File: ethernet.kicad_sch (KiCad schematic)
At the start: 43 parts, among them J4 ARJM11D7-502-AB-EW2, U1 MIMX8MM6DVTLZAA, U13 TPD4EUSB30, U14 TPD4EUSB30, U18 RTL8211FD

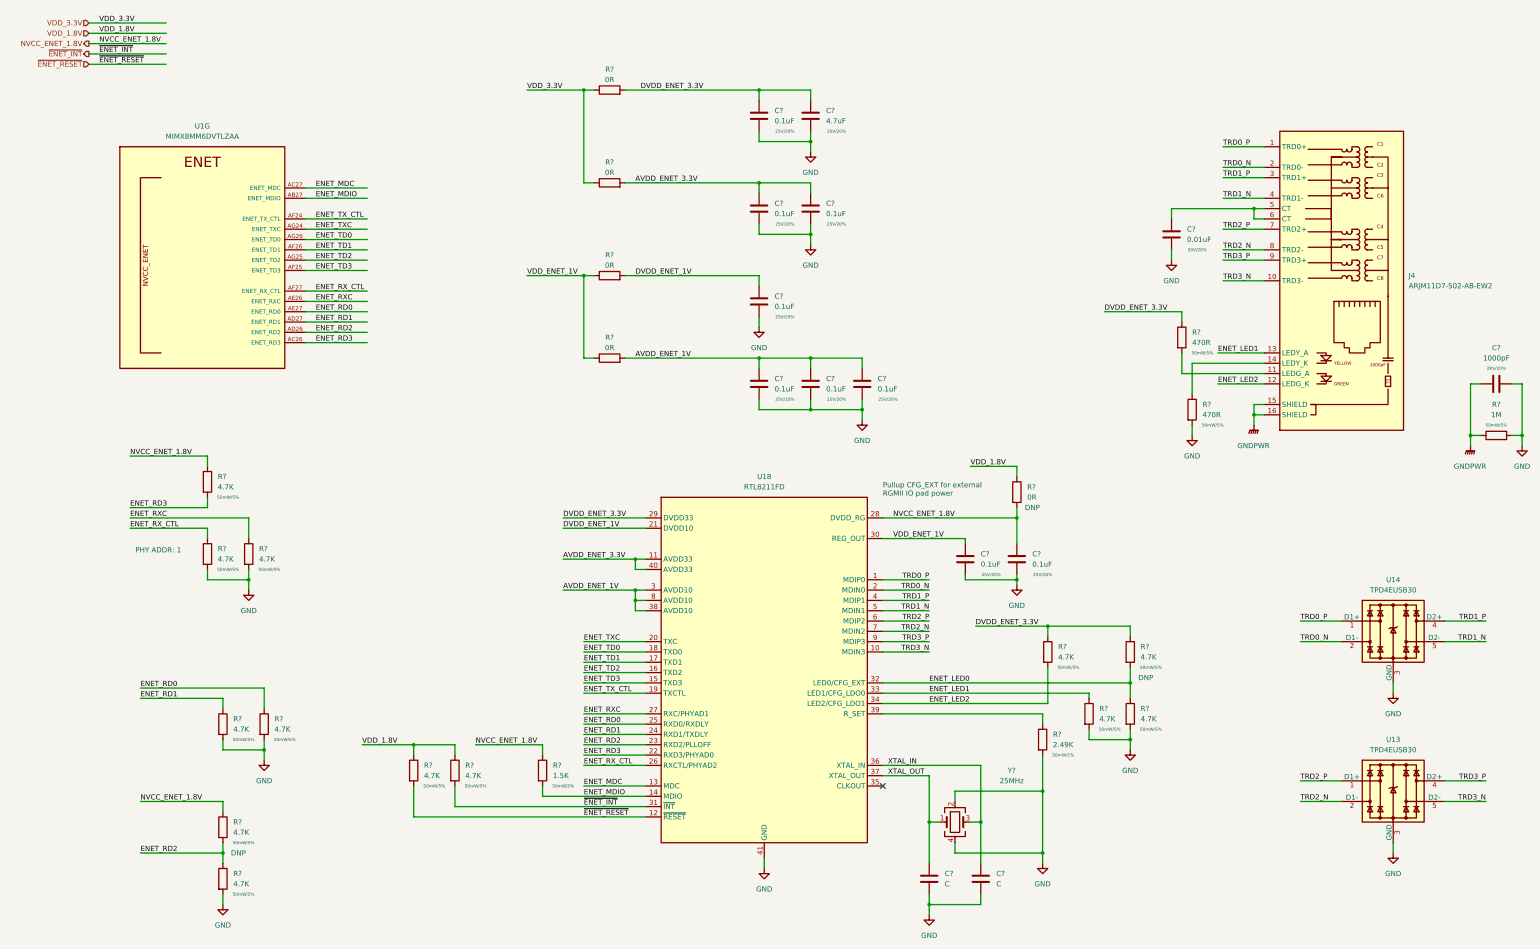
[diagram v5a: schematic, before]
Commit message: pcie done, misc fixes for usb, enet
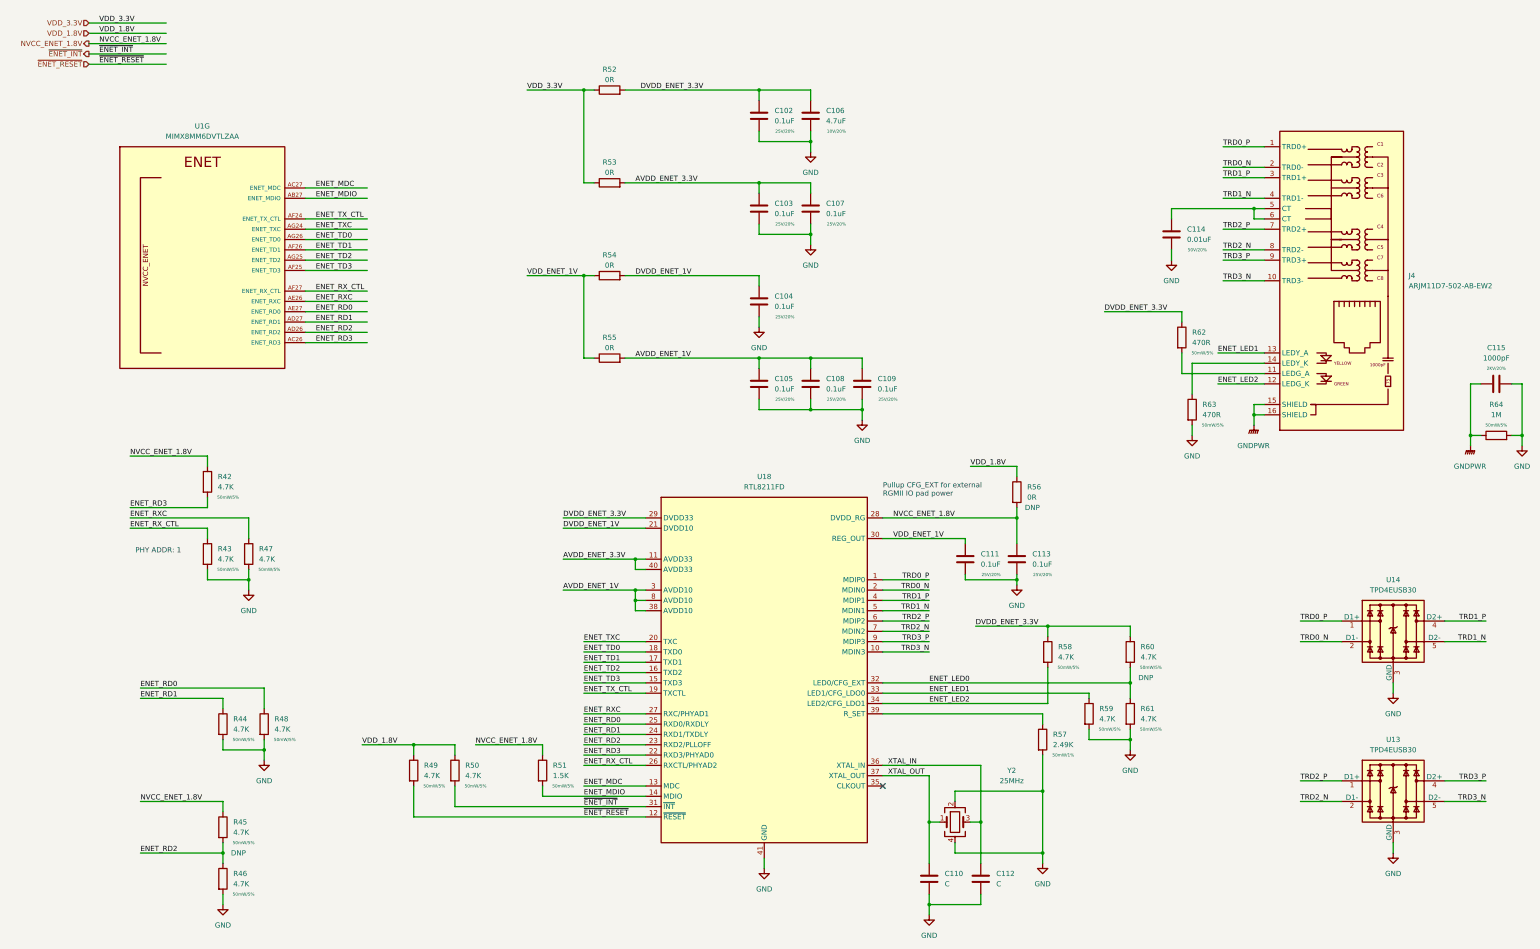
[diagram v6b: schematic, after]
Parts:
- gave numbers to parts that had none: 38

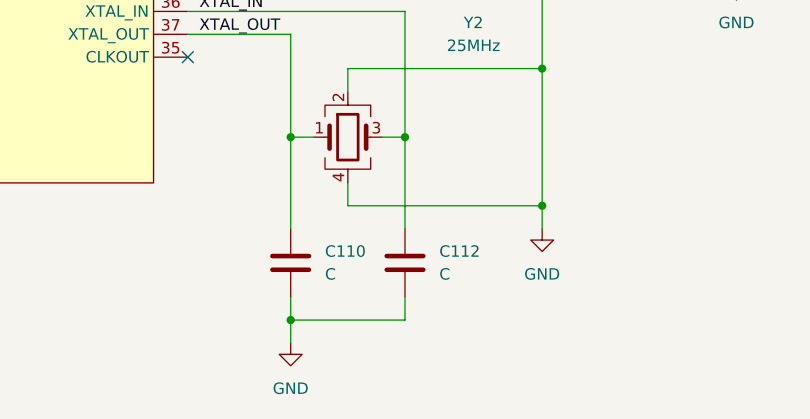
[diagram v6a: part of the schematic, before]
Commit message: ddr: add dual die support, misc work
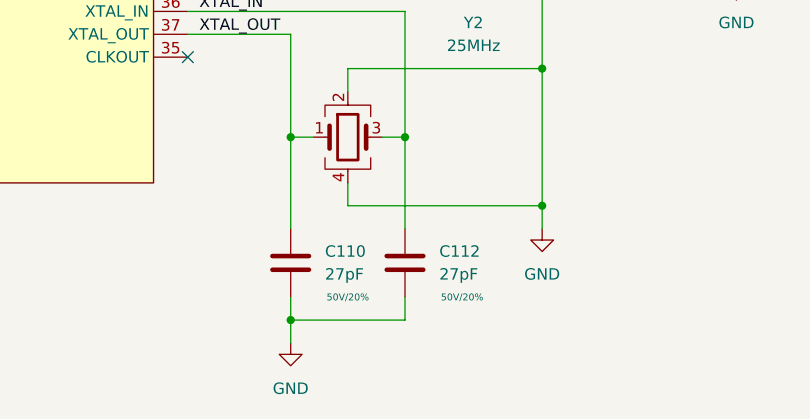
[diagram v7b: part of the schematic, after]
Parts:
- C110, C112: value C -> 27pF; Rating (none) -> 50V/20%
- Y2: footprint (none) -> Crystal:Crystal_SMD_3225-4Pin_3.2x2.5mm
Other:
- company: (none) -> Q-LAB
- title: (none) -> QSBC
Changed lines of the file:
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@@
 (kicad_sch (version 20211123) (generator eeschema)
   (paper "A3")
+  (title_block
+    (title "QSBC")
+    (rev "1")
+    (company "Q-LAB")
+  )
   (junction (at 210.82 115.57) (diameter 0) (color 0 0 0 0)
   )
@@
     )
     (pin "1")
+  )
+  (symbol (lib_id "Device:C") (at 240.03 231.14 0) (unit 1)
+    (in_bom yes) (on_board yes)
+    (property "Reference" "C110" (id 0) (at 243.84 229.8699 0)
+      (effects (font (size 1.27 1.27)) (justify left))
+    )
+    (property "Value" "27pF" (id 1) (at 243.84 232.4099 0)
+      (effects (font (size 1.27 1.27)) (justify left))
+    )
+    (property "Footprint" "Capacitor_SMD:C_0402_1005Metric" (id 2) (at 240.9952 234.95 0)
+      (effects (font (size 1.27 1.27)) hide)
+    )
+    (property "Datasheet" "~" (id 3) (at 240.03 231.14 0)
+      (effects (font (size 1.27 1.27)) hide)
+    )
+    (property "Rating" "50V/20%" (id 4) (at 246.38 234.95 0)
+      (effects (font (size 0.762 0.762)))
+    )
+    (pin "1")
+    (pin "2")
   )
   (symbol (lib_id "power:GND") (at 210.82 74.93 0) (unit 1)
@@
     (pin "9")
   )
-  (symbol (lib_id "Device:C") (at 240.03 231.14 0) (unit 1)
-    (in_bom yes) (on_board yes) (fields_autoplaced)
-    (property "Reference" "C110" (id 0) (at 243.84 229.8699 0)
-      (effects (font (size 1.27 1.27)) (justify left))
-    )
-    (property "Value" "C" (id 1) (at 243.84 232.4099 0)
-      (effects (font (size 1.27 1.27)) (justify left))
-    )
-    (property "Footprint" "Capacitor_SMD:C_0402_1005Metric" (id 2) (at 240.9952 234.95 0)
-      (effects (font (size 1.27 1.27)) hide)
-    )
-    (property "Datasheet" "~" (id 3) (at 240.03 231.14 0)
-      (effects (font (size 1.27 1.27)) hide)
-    )
-    (pin "1")
-    (pin "2")
-  )
   (symbol (lib_id "Device:R") (at 161.29 102.87 90) (unit 1)
     (in_bom yes) (on_board yes)
@@
     (property "Reference" "Y2" (id 0) (at 260.35 204.47 0))
     (property "Value" "25MHz" (id 1) (at 260.35 207.01 0))
-    (property "Footprint" "" (id 2) (at 246.38 217.17 0)
+    (property "Footprint" "Crystal:Crystal_SMD_3225-4Pin_3.2x2.5mm" (id 2) (at 246.38 217.17 0)
       (effects (font (size 1.27 1.27)) hide)
     )
@@
   )
   (symbol (lib_id "Device:C") (at 252.73 231.14 0) (unit 1)
-    (in_bom yes) (on_board yes) (fields_autoplaced)
+    (in_bom yes) (on_board yes)
     (property "Reference" "C112" (id 0) (at 256.54 229.8699 0)
       (effects (font (size 1.27 1.27)) (justify left))
     )
-    (property "Value" "C" (id 1) (at 256.54 232.4099 0)
+    (property "Value" "27pF" (id 1) (at 256.54 232.4099 0)
       (effects (font (size 1.27 1.27)) (justify left))
     )
@@
       (effects (font (size 1.27 1.27)) hide)
     )
-    (pin "1")
+    (property "Rating" "50V/20%" (id 4) (at 259.08 234.95 0)
+      (effects (font (size 0.762 0.762)))
+    )
+    (pin "1")

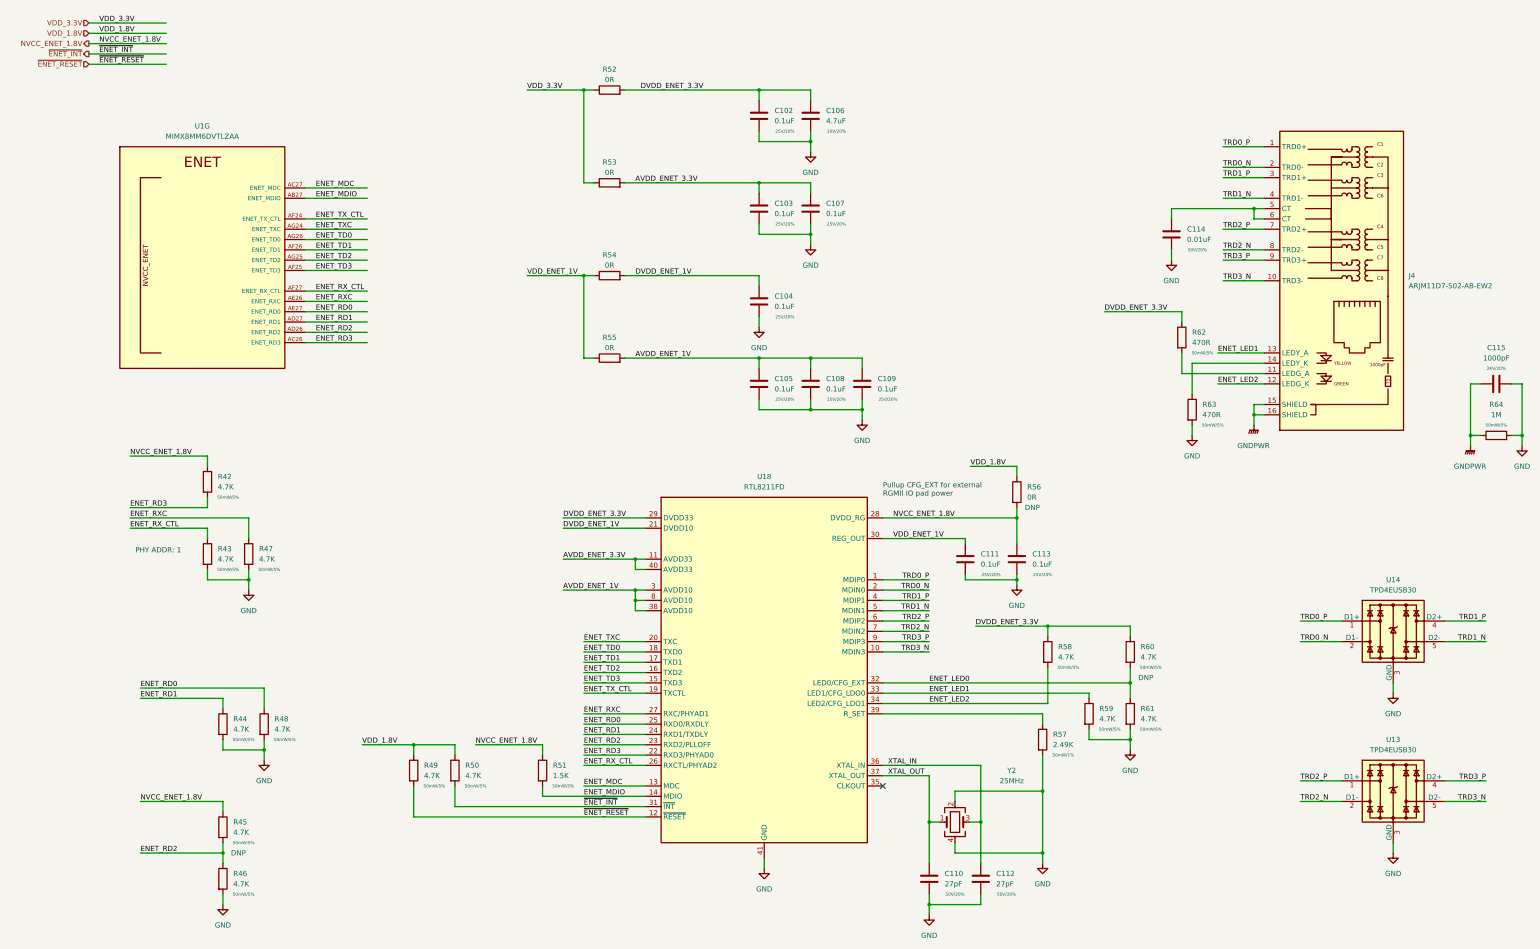
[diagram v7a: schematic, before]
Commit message: fix ref desgigators, add table for dram config
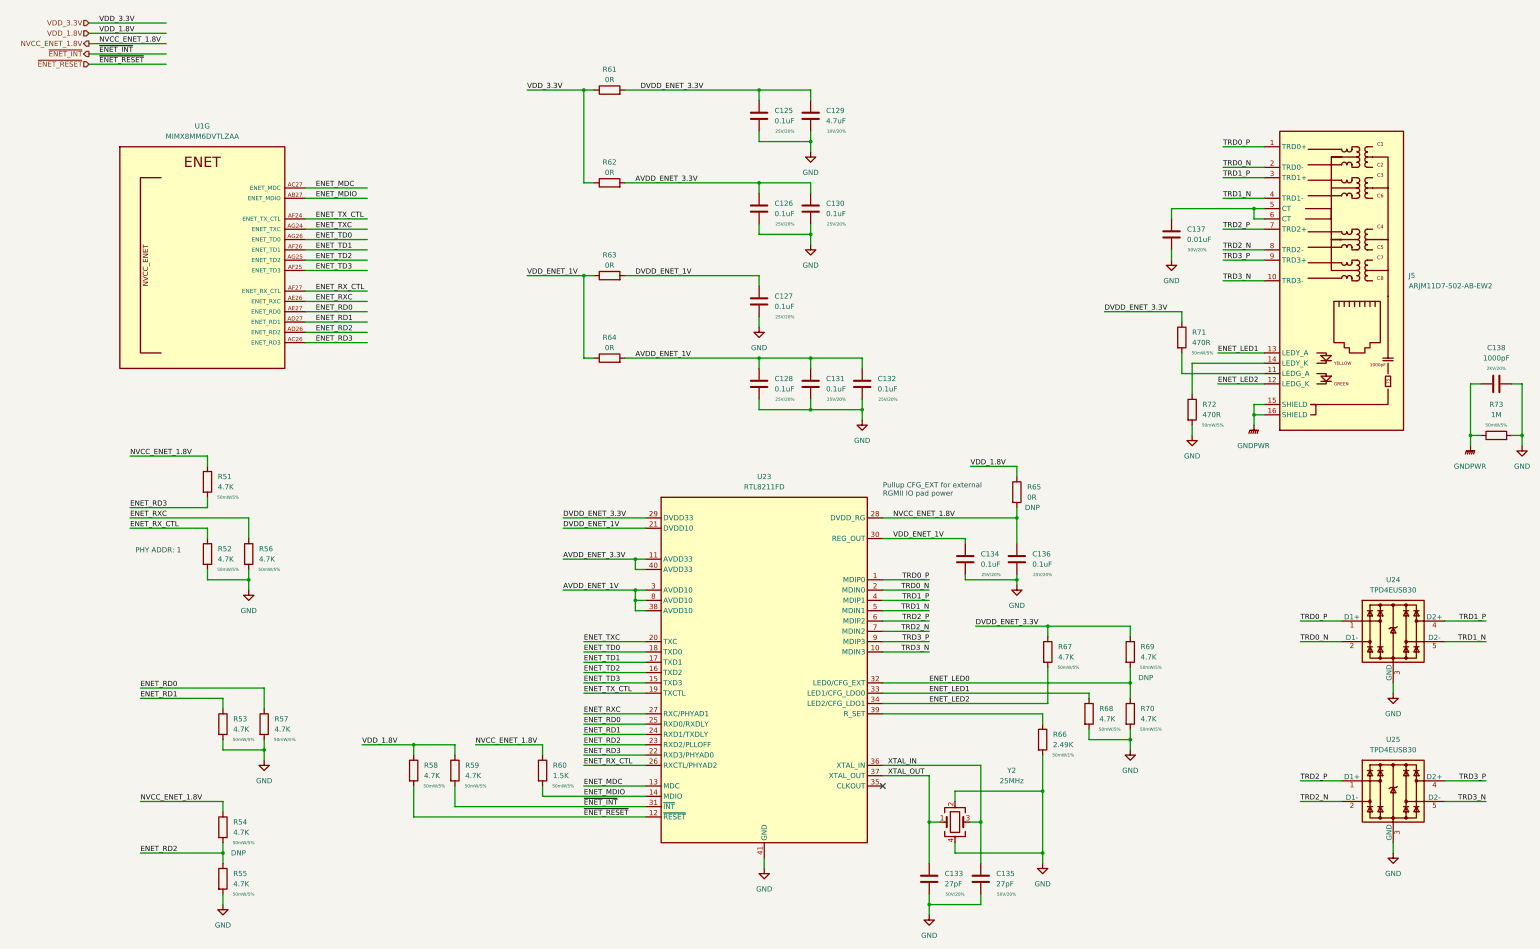
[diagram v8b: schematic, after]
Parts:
- renumbered C102 to C125, C103 to C126, C104 to C127, C105 to C128, C106 to C129, C107 to C130, C108 to C131, C109 to C132, C110 to C133, C111 to C134, C112 to C135, C113 to C136, C114 to C137, C115 to C138, J4 to J5, R42 to R51, R43 to R52, R44 to R53, R45 to R54, R46 to R55, R47 to R56, R48 to R57, R49 to R58, R50 to R59, R51 to R60, R52 to R61, R53 to R62, R54 to R63, R55 to R64, R56 to R65, R57 to R66, R58 to R67, R59 to R68, R60 to R69, R61 to R70, R62 to R71, R63 to R72, R64 to R73, U18 to U23, U14 to U24, U13 to U25
